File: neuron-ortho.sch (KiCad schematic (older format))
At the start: 138 parts, among them J1 USB_C_Receptacle, J2 Conn_01x04_Male, J3 Conn_01x06_Male, J4 Conn_01x04_Male, J5 Conn_01x04_Male, Q1 DTC123J, SW1 SW_Push, U1 STM32F303C6Tx, U2 NCP1117-3.3_SOT223, U3 USBLC6-2SC6, Y1 8MHz

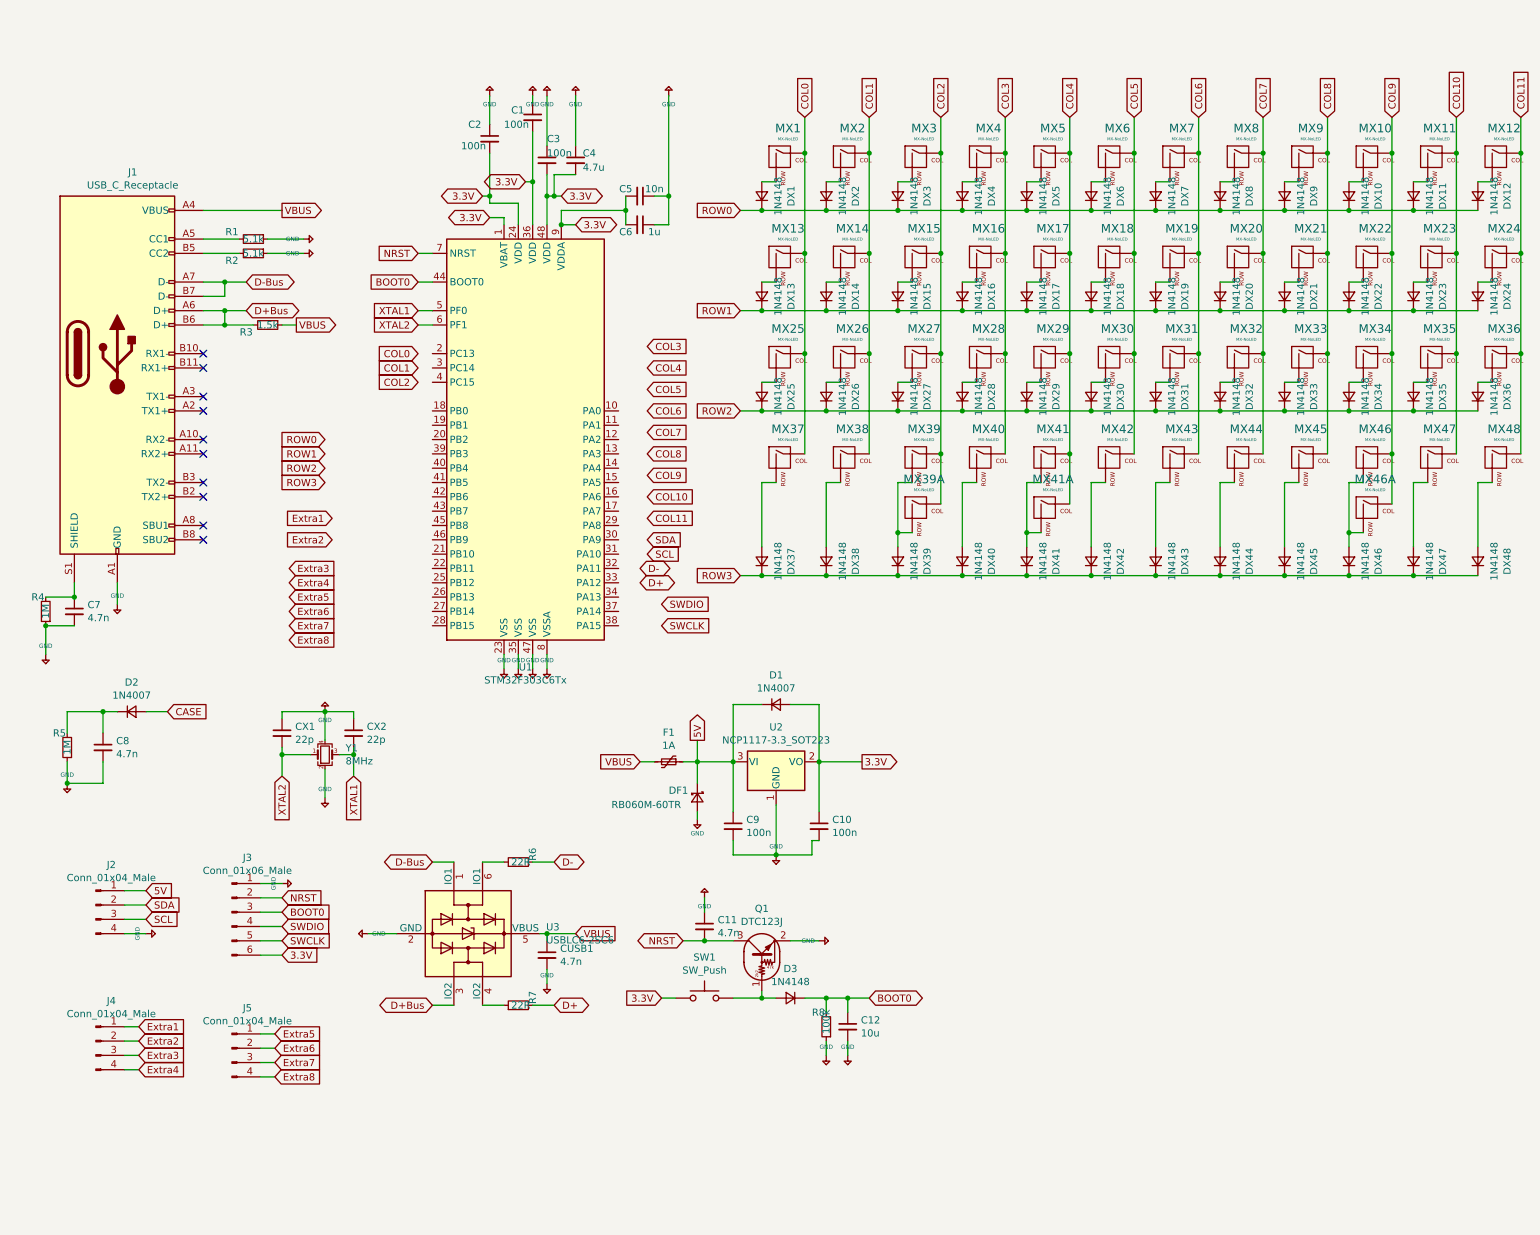
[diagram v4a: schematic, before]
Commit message: Completed PCB trace
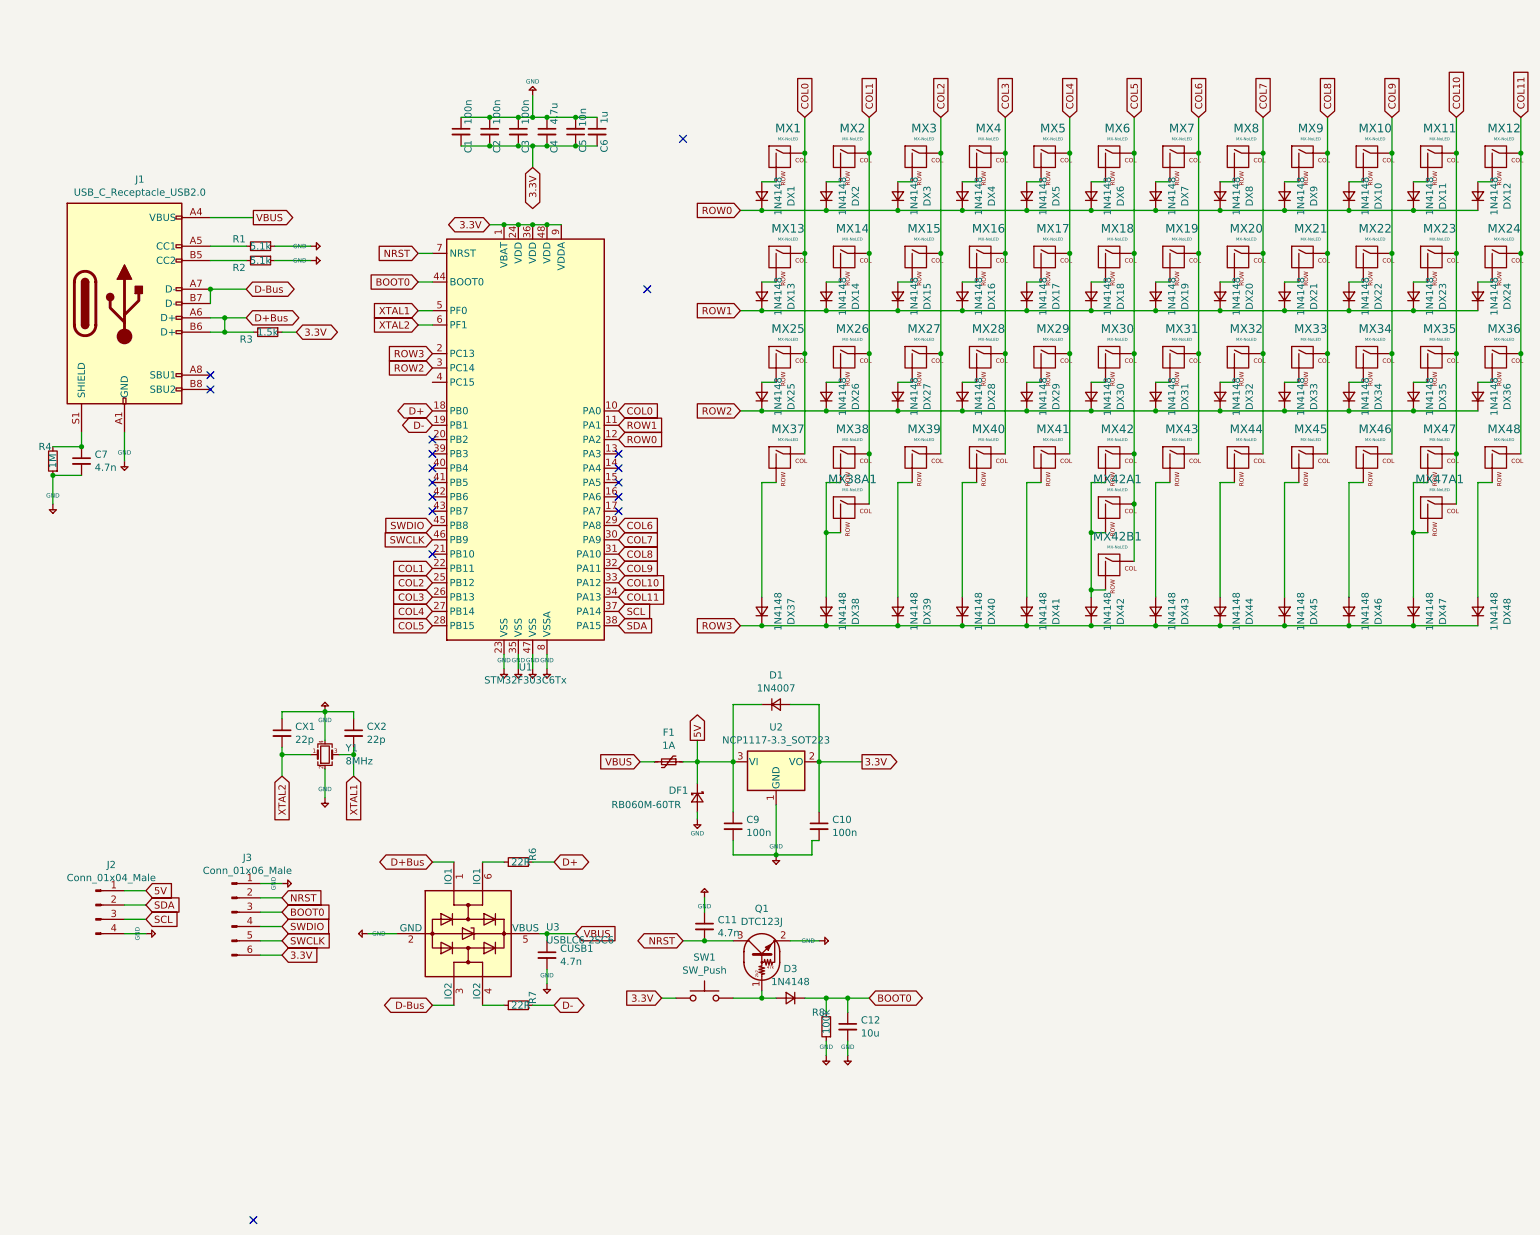
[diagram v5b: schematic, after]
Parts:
- removed C8: 4.7n, symbol Device:C_Small
- removed D2: 1N4007, symbol Device:D_Small
- removed J1: USB_C_Receptacle, symbol Connector:USB_C_Receptacle
- removed J4, J5: Conn_01x04_Male, symbol Connector:Conn_01x04_Male
- removed R5: 1M, symbol Device:R_Small
- added J1: USB_C_Receptacle_USB2.0, Connector_USB:USB_C_Receptacle_GCT_USB4085, symbol Connector:USB_C_Receptacle_USB2.0
- added MX42B1: MX-NoLED, MX_Alps_Hybrid:MX-2U-ReversedStabilizers-NoLED, symbol MX_Alps_Hybrid:MX-NoLED
- C1, C10, C11, C12, C2, C3, C4, C5, C6, C7, C9, CUSB1, CX1, CX2: footprint (none) -> Capacitor_SMD:C_0805_2012Metric
- D1, D3, DF1, DX1, DX10, DX11, DX12, DX13, DX14, DX15, DX16, DX17, DX18, DX19, DX2, DX20, DX21, DX22, DX23, DX24, DX25, DX26, DX27, DX28, DX29, DX3, DX30, DX31, DX32, DX33, DX34, DX35, DX36, DX37, DX38, DX39, DX4, DX40, DX41, DX42, DX43, DX44, DX45, DX46, DX47, DX48, DX5, DX6, DX7, DX8, DX9: footprint (none) -> Diode_SMD:D_SOD-123
- F1: footprint (none) -> Fuse:Fuse_1206_3216Metric
- J2: footprint (none) -> Connector_PinSocket_1.00mm:PinSocket_1x04_P1.00mm_Vertical
- J3: footprint (none) -> Connector_PinSocket_1.00mm:PinSocket_1x06_P1.00mm_Vertical
- MX1, MX10, MX11, MX12, MX13, MX14, MX15, MX16, MX17, MX18, MX19, MX2, MX20, MX21, MX22, MX23, MX24, MX25, MX26, MX27, MX28, MX29, MX3, MX30, MX31, MX32, MX33, MX34, MX35, MX36, MX37, MX38, MX39, MX4, MX40, MX41, MX42, MX43, MX44, MX45, MX46, MX47, MX48, MX5, MX6, MX7, MX8, MX9: footprint (none) -> MX_Alps_Hybrid:MX-1U-NoLED
- MX38A1: renamed from MX39A; footprint (none) -> MX_Alps_Hybrid:MX-1.5U-NoLED
- MX42A1: renamed from MX41A; footprint (none) -> MX_Alps_Hybrid:MX-7U-ReversedStabilizers-NoLED
- MX47A1: renamed from MX46A; footprint (none) -> MX_Alps_Hybrid:MX-1.5U-NoLED
- Q1: footprint (none) -> Package_TO_SOT_SMD:SOT-23
- R1, R2, R3, R4, R6, R7, R8: footprint (none) -> Resistor_SMD:R_0805_2012Metric
- SW1: footprint (none) -> random-keyboard-parts:SKQG-1155865
- Y1: footprint (none) -> Crystal:Crystal_SMD_3225-4Pin_3.2x2.5mm
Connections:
- net +5V: now also C5.2, J1.A1 (GND), J1.A12 (GND), J1.B1 (GND), J1.B12 (GND); no longer C5.1
- net 3.3V: now also C5.1, R3.1; no longer C5.2
- net COL0: now also U1.10 (PA0)
- net COL1: now also MX38A1.1 (COL), U1.22 (PB11)
- net COL10: now also MX47A1.1 (COL), U1.33 (PA12)
- net COL11: now also U1.34 (PA13)
- net COL2: now also U1.25 (PB12); no longer MX38A1.1 (COL)
- net COL3: now also U1.26 (PB13)
- net COL4: now also U1.27 (PB14); no longer MX42A1.1 (COL)
- net COL5: now also MX42A1.1 (COL), U1.28 (PB15), MX42B1.1 (COL)
- net COL6: now also U1.29 (PA8)
- net COL7: now also U1.30 (PA9)
- net COL8: now also U1.31 (PA10)
- net COL9: now also U1.32 (PA11); no longer MX47A1.1 (COL)
- net D+: now also R6.2, U1.18 (PB0); no longer R7.2
- net D+Bus: now also U3.1 (IO1), J1.A6 (D+), J1.B6 (D+); no longer U3.3 (IO2)
- net D-: now also R7.2, U1.19 (PB1); no longer R6.2
- net D-Bus: now also U3.3 (IO2), J1.A7 (D-), J1.B7 (D-); no longer U3.1 (IO1)
- net ROW0: now also U1.12 (PA2)
- net ROW1: now also U1.11 (PA1)
- net ROW2: now also U1.3 (PC14)
- net ROW3: now also U1.2 (PC13)
- net SCL: now also U1.37 (PA14)
- net SDA: now also U1.38 (PA15)
- net SWCLK: now also U1.46 (PB9)
- net SWDIO: now also U1.45 (PB8)
- net VBUS: now also J1.A4 (VBUS), J1.A9 (VBUS), J1.B4 (VBUS), J1.B9 (VBUS); no longer R3.1
- net at R1.2: now also J1.A5 (CC1)
- net at R2.2: now also J1.B5 (CC2)
- net at C7.1, R4.2: now also J1.S1 (SHIELD)
- net at DX38.2 (A), MX38.2 (ROW): now also MX38A1.2 (ROW)
- net at DX42.2 (A), MX42.2 (ROW): now also MX42A1.2 (ROW), MX42B1.2 (ROW)
- net at DX46.2 (A), MX46.2 (ROW): no longer MX47A1.2 (ROW)
- net at DX47.2 (A), MX47.2 (ROW): now also MX47A1.2 (ROW)
- net at DX39.2 (A), MX39.2 (ROW): no longer MX38A1.2 (ROW)
- net at DX41.2 (A), MX41.2 (ROW): no longer MX42A1.2 (ROW)
- no-connect marks 10 -> 17
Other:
- moved on the sheet: C1, C2, C3, C4, C5, C6, C7, DX37, DX38, DX39, DX40, DX41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
